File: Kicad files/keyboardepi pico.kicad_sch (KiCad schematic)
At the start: 135 parts, among them U1 Raspberry_Pi_Pico

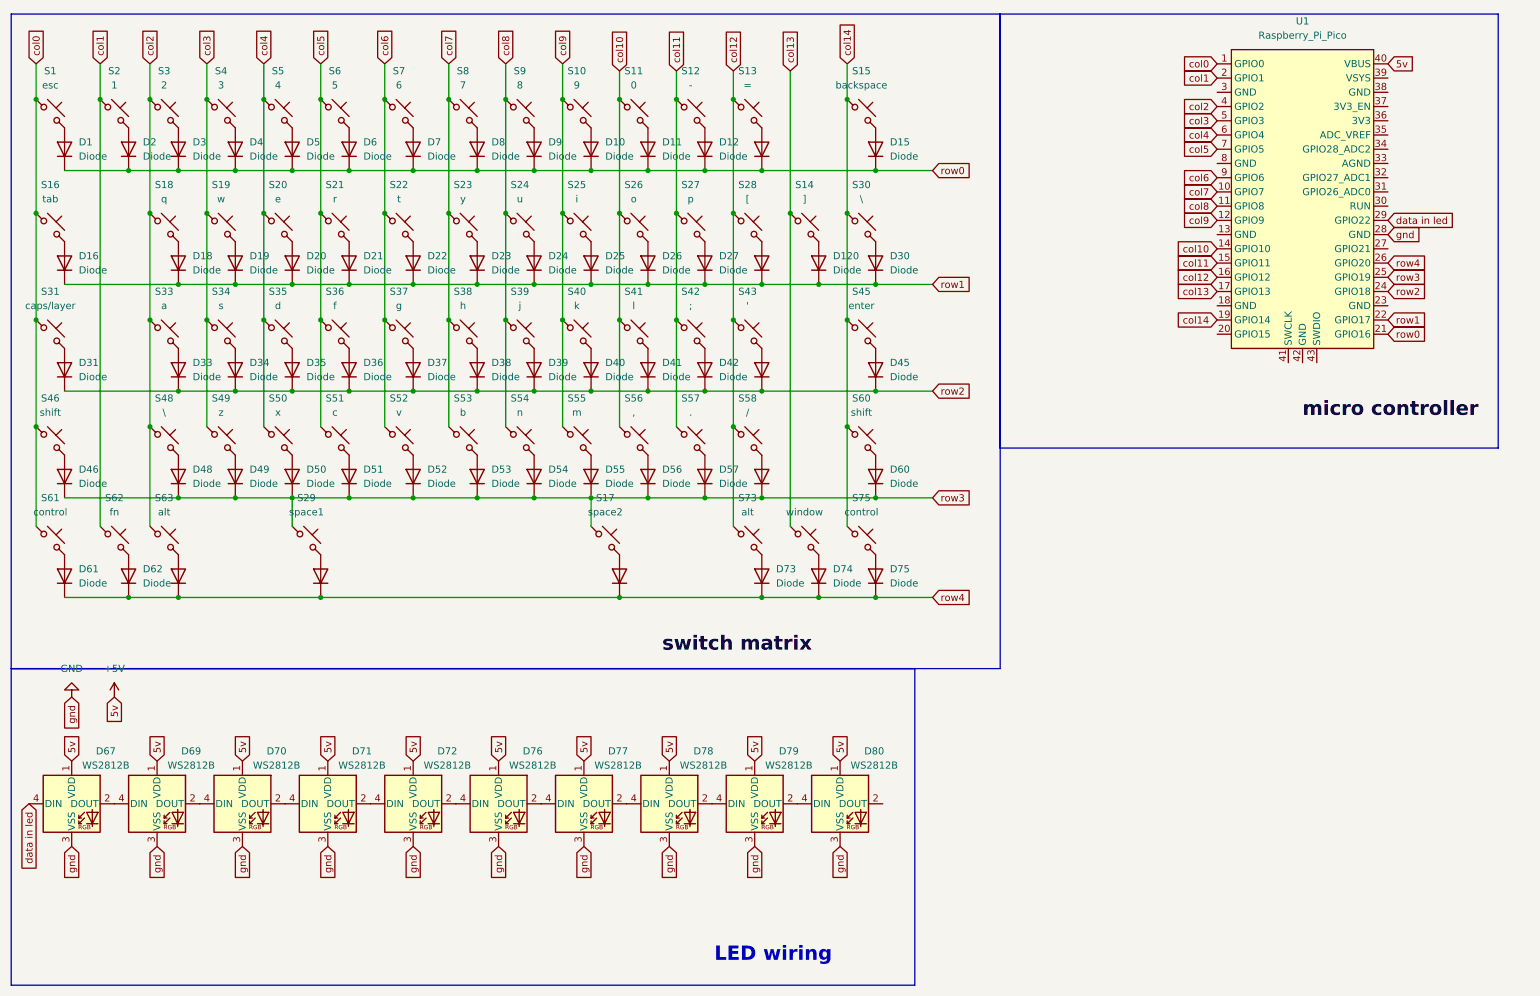
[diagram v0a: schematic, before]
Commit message: Removed the LEDs
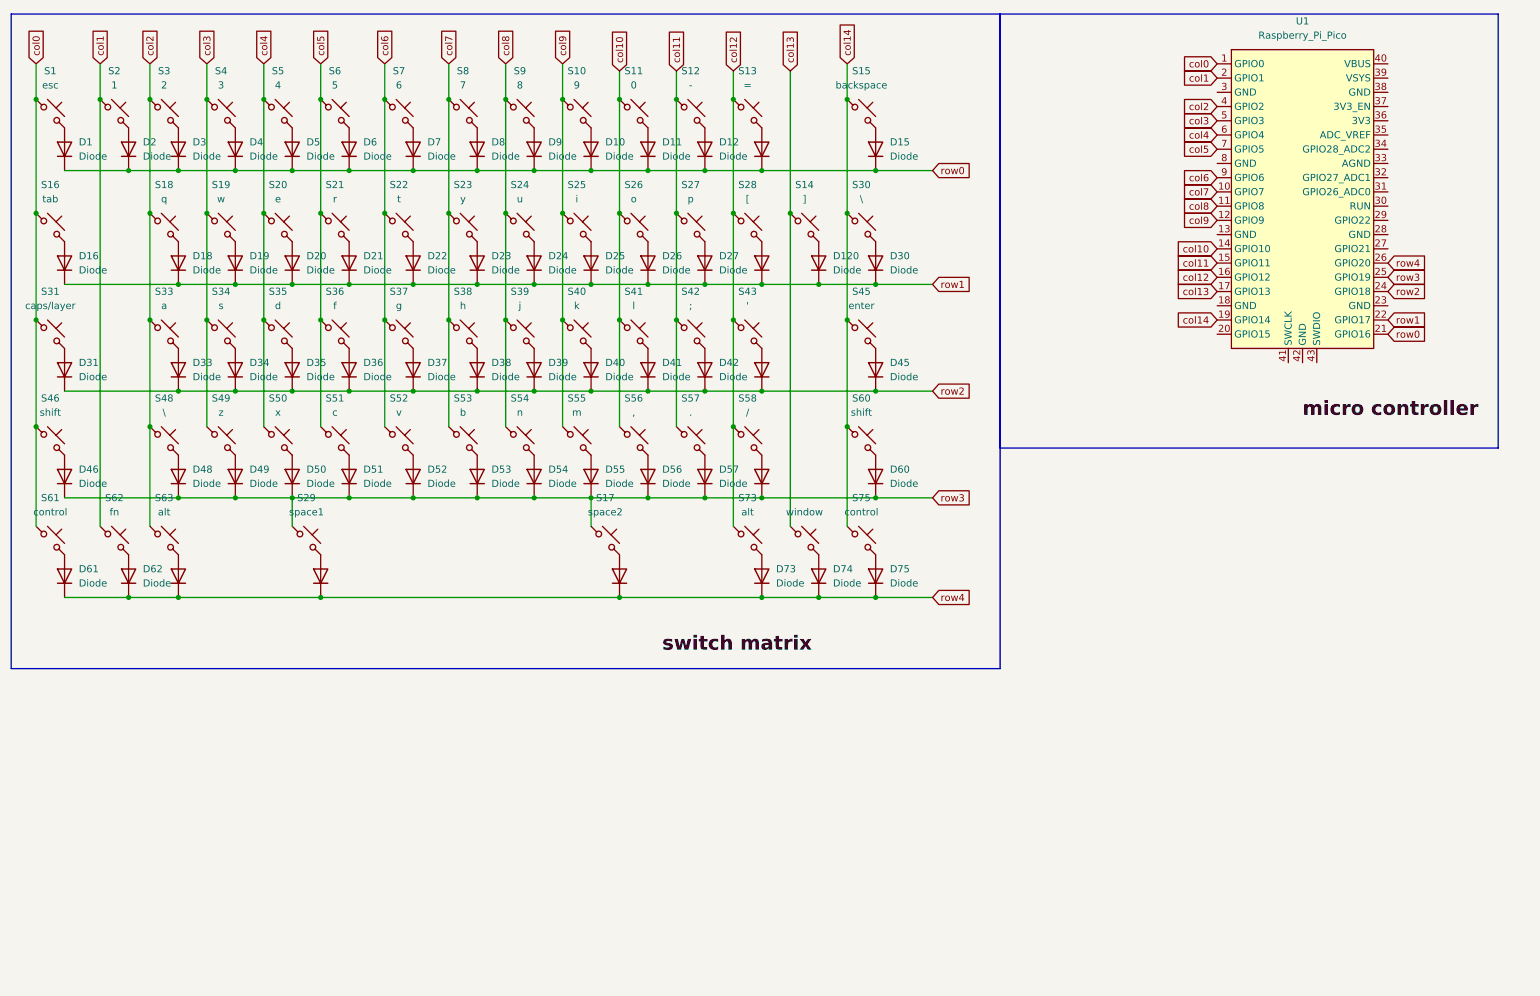
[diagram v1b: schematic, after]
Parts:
- removed D67, D69, D70, D71, D72, D76, D77, D78, D79, D80: WS2812B, LED_SMD:LED_WS2812B_PLCC4_5.0x5.0mm_P3.2mm, symbol LED:WS2812B
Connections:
- net +5V: no longer names the net of U1.40 (VBUS)
- net GND: no longer names the net of U1.28 (GND)
- net data in led: no longer names the net of U1.29 (GPIO22)
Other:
- note removed: "LED wiring"

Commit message: finishing up to ship the project
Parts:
- added D14, D17, D29, D32, D44, D47, D59, D64, D65, D66: WS2812B, LED_SMD:LED_WS2812B_PLCC4_5.0x5.0mm_P3.2mm, symbol LED:WS2812B
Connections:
- net Data in LED: now reaches U1.29 (GPIO22)
- net Data in LED: now also D14.4 (DIN)
- net GND: now reaches U1.38 (GND)
- net GND: now also D14.3 (VSS), D17.3 (VSS), D29.3 (VSS), D32.3 (VSS), D44.3 (VSS), D47.3 (VSS), D59.3 (VSS), D64.3 (VSS), D65.3 (VSS), D66.3 (VSS)
- net +5V: now reaches U1.40 (VBUS)
- net +5V: now also D14.1 (VDD), D17.1 (VDD), D29.1 (VDD), D32.1 (VDD), D44.1 (VDD), D47.1 (VDD), D59.1 (VDD), D64.1 (VDD), D65.1 (VDD), D66.1 (VDD)
- new net: D14.2 (DOUT), D17.4 (DIN)
- new net: D17.2 (DOUT), D29.4 (DIN)
- new net: D44.2 (DOUT), D47.4 (DIN)
- new net: D32.2 (DOUT), D44.4 (DIN)
- new net: D65.2 (DOUT), D66.4 (DIN)
- new net: D29.2 (DOUT), D32.4 (DIN)
- new net: D59.2 (DOUT), D64.4 (DIN)
- new net: D47.2 (DOUT), D59.4 (DIN)
- new net: D64.2 (DOUT), D65.4 (DIN)

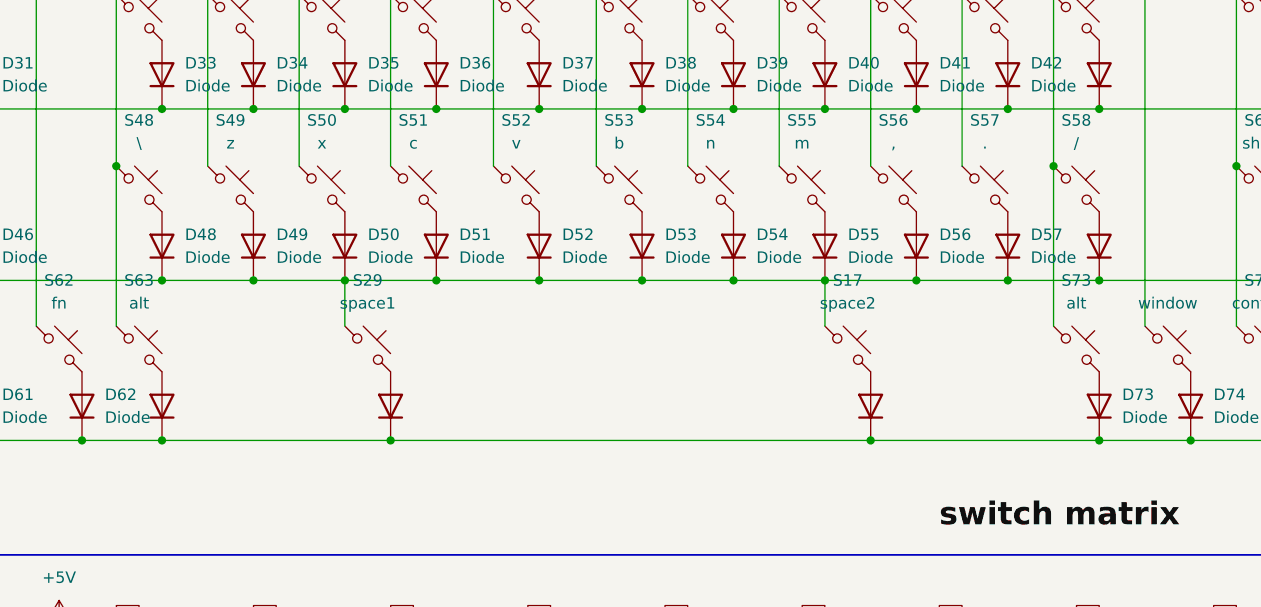
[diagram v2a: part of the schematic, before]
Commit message: rebuilding gbr files and pcb for better soldering ease
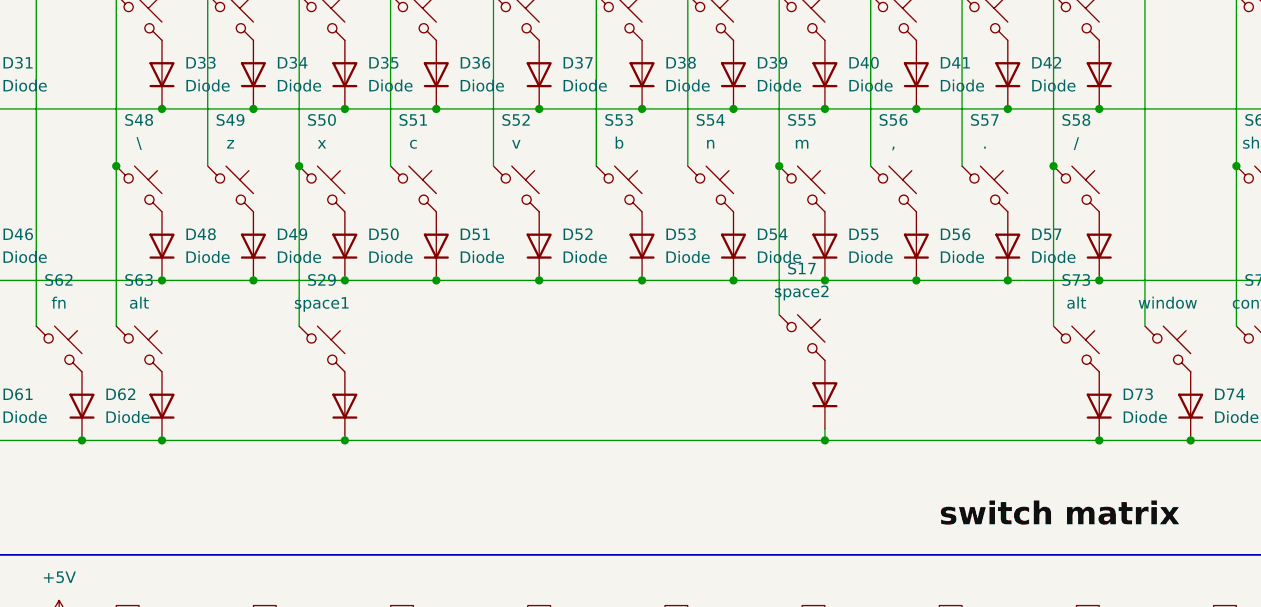
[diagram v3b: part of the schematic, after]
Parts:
- D1, D10, D11, D12, D120, D121, D13, D15, D16, D18, D19, D2, D20, D21, D22, D23, D24, D25, D26, D27, D28, D3, D30, D31, D33, D34, D35, D36, D37, D38, D39, D4, D40, D41, D42, D43, D45, D46, D48, D49, D5, D50, D51, D52, D53, D54, D55, D56, D57, D58, D6, D60, D61, D62, D63, D68, D7, D73, D74, D75, D8, D9: footprint Diode_SMD:D_SOD-123F -> ScottoKeebs_Components:Diode_DO-35
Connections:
- net col4: now also S29.1
- net col9: now also S17.1
- net row3: no longer S17.1, S29.1
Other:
- moved on the sheet: S17, S29
